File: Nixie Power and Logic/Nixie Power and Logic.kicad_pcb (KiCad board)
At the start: 2 copper layers, 172.7 x 111.8 mm, 54 parts, among them J1 Barrel_Jack, J10 Conn_01x20_Female, J11 Conn_01x20_Female, J12 Conn_01x20_Female, J13 LED Data, J2 Conn_01x02_Female, J3 Conn_01x02_Female, J4 Conn_01x02_Female, J5 Conn_01x02_Female, J6 Conn_01x02_Female, J7 Conn_01x02_Female, J8 Programming, J9 RTC, Q1 IRF740, Q2 MPSA92, Q3 BC547, SW1 SW_SPST, SW2 SW_SPST, SW3 Rotary_Encoder_EN11, SW4 Rotary_Encoder_EN11, SW5 Rotary_Encoder_EN11, SW6 SW_Reset, U1 ATmega168PA-PU, U10 74141, U11 L7805, U12 NE555, U2 74HC595, U3 74HC595, U4 74HC595, U5 74141, U6 74141, U7 74141, U8 74141, U9 74141, Y1 20MHz

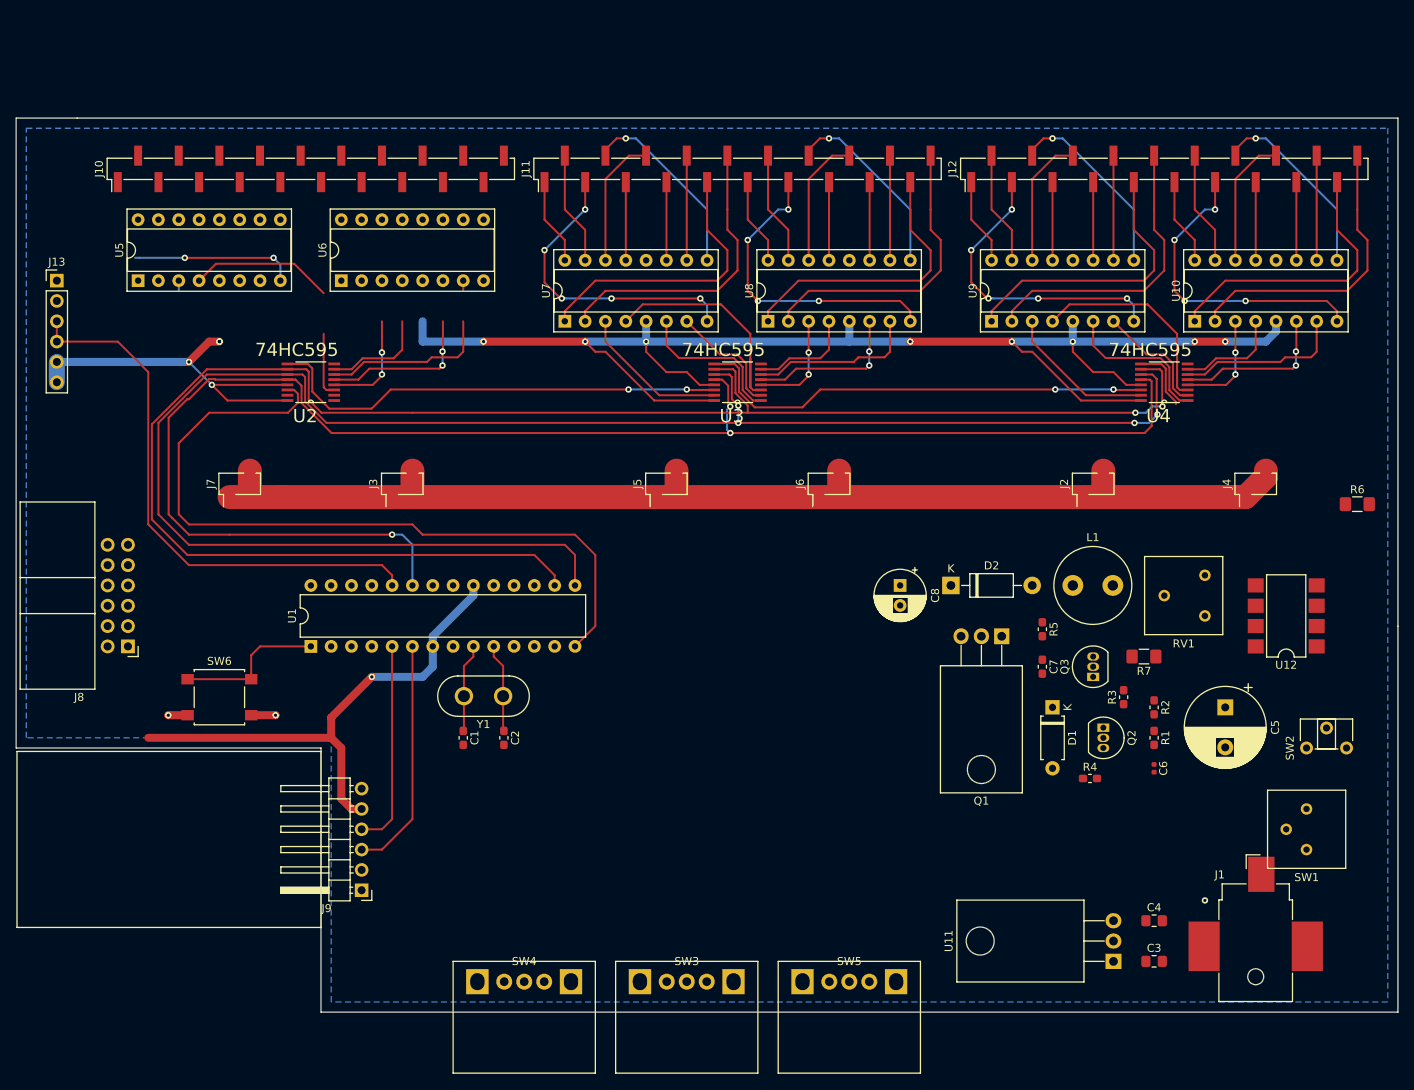
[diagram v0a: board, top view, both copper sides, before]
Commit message: Final V1.0 design. Different sized boards for top and bottom layer. Goal for v2.0 is to have matching top and bottom pcbas
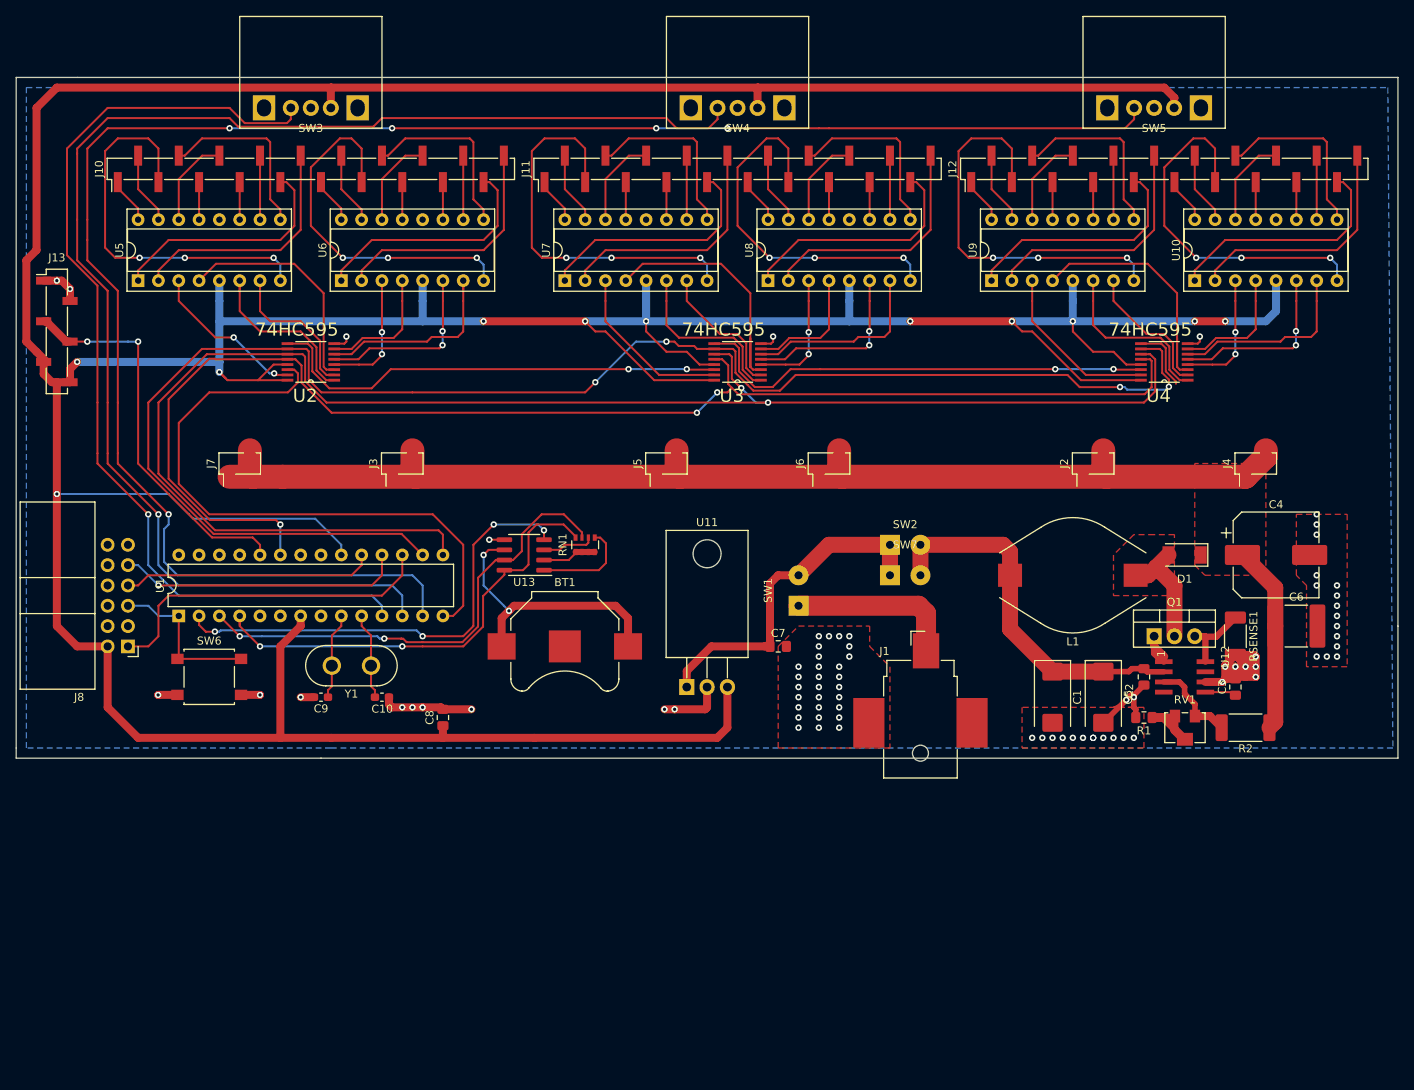
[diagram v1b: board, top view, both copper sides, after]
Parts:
- removed D2: uf4007, Diode_THT:D_DO-41_SOD81_P10.16mm_Horizontal
- removed J9: RTC, Connector_PinHeader_2.54mm:PinHeader_1x06_P2.54mm_Horizontal
- removed Q2: MPSA92, Package_TO_SOT_THT:TO-92_Inline
- removed Q3: BC547, Package_TO_SOT_THT:TO-92_Inline
- removed R3: 33k, Resistor_SMD:R_0603_1608Metric_Pad1.05x0.95mm_HandSolder
- removed R4, R5: 1k, Resistor_SMD:R_0603_1608Metric_Pad1.05x0.95mm_HandSolder
- removed R6: 220k, Resistor_SMD:R_1206_3216Metric_Pad1.42x1.75mm_HandSolder
- removed R7: 470, Resistor_SMD:R_1206_3216Metric_Pad1.42x1.75mm_HandSolder
- added BT1: Battery_Cell, Battery:BatteryHolder_Keystone_3000_1x12mm, F.Cu at (172.7, 85.1)
- added C1: 100Uf 35V, Capacitor_Tantalum_SMD:CP_EIA-7343-31_Kemet-D_Pad2.25x2.55mm_HandSolder, F.Cu at (233.7, 91.4)
- added C2: 100n, Capacitor_SMD:C_0805_2012Metric_Pad1.15x1.40mm_HandSolder, F.Cu at (245.1, 88.9)
- added RN1: R_Pack04, Resistor_SMD:R_Array_Convex_4x0603, F.Cu at (175.3, 72.4)
- added RSENSE1: 0R050, Resistor_SMD:R_2010_5025Metric_Pad1.52x2.65mm_HandSolder, F.Cu at (256.5, 83.8)
- added SW7: SW_Reset, Connector_Wire:SolderWirePad_1x02_P3.81mm_Drill1mm, F.Cu at (213.4, 76.2)
- added U13: DS3231MZ, Package_SO:SOIC-8_3.9x4.9mm_P1.27mm, F.Cu at (167.6, 73.7)
- C10: renamed from C2; value C -> 22pF
- C3: value 0.33uF -> 100n
- C4: value 0.1uF -> 4u7 250V; footprint Capacitor_SMD:C_0805_2012Metric_Pad1.15x1.40mm_HandSolder -> Capacitor_SMD:CP_Elec_10x14.3
- C5: value 470uF -> 10uF 25V; footprint Capacitor_THT:CP_Radial_D10.0mm_P5.00mm -> Capacitor_Tantalum_SMD:CP_EIA-7343-31_Kemet-D_Pad2.25x2.55mm_HandSolder
- C6: value 2n2 -> 100n 250V; footprint Capacitor_SMD:C_0402_1005Metric -> Capacitor_SMD:C_2220_5650Metric_Pad1.97x5.40mm_HandSolder
- C7: value 47pF -> 0.33uF; footprint Capacitor_SMD:C_0603_1608Metric_Pad1.05x0.95mm_HandSolder -> Capacitor_SMD:C_0805_2012Metric_Pad1.15x1.40mm_HandSolder
- C8: value 1uF 350V -> 0.1uF; footprint Capacitor_THT:CP_Radial_D6.3mm_P2.50mm -> Capacitor_SMD:C_0805_2012Metric_Pad1.15x1.40mm_HandSolder
- C9: renamed from C1; value C -> 22pF
- D1: value 1n914 -> ES2F; footprint Diode_THT:D_A-405_P7.62mm_Horizontal -> Nixie Power and Logic:D_SOD-214AA
- J13: footprint Connector_PinHeader_2.54mm:PinHeader_1x06_P2.54mm_Vertical -> Connector_PinSocket_2.54mm:PinSocket_1x06_P2.54mm_Vertical_SMD_Pin1Left
- L1: footprint Inductor_THT:L_Radial_D9.5mm_P5.00mm_Fastron_07HVP -> Inductor_SMD:L_Bourns_SDR1806
- Q1: value IRF740 -> IRF644; footprint Package_TO_SOT_THT:TO-220-3_Horizontal_TabDown -> Package_TO_SOT_THT:TO-220-3_Vertical
- R1: footprint Resistor_SMD:R_0603_1608Metric_Pad1.05x0.95mm_HandSolder -> Resistor_SMD:R_0805_2012Metric_Pad1.15x1.40mm_HandSolder
- R2: value 1k -> 1M5; footprint Resistor_SMD:R_0603_1608Metric_Pad1.05x0.95mm_HandSolder -> Resistor_SMD:R_2512_6332Metric_Pad1.52x3.35mm_HandSolder
- RV1: value 1k -> 5k; footprint Potentiometer_THT:Potentiometer_Bourns_3386F_Vertical -> Potentiometer_SMD:Potentiometer_Bourns_3214W_Vertical
- SW1: value SW_SPST -> Main Power Switch; footprint Potentiometer_THT:Potentiometer_Bourns_3386P_Vertical -> Connector_Wire:SolderWirePad_1x02_P3.81mm_Drill1mm
- SW2: value SW_SPST -> 180V Switch; footprint Potentiometer_THT:Potentiometer_Piher_PT-6-H_Horizontal -> Connector_Wire:SolderWirePad_1x02_P3.81mm_Drill1mm
- U12: value NE555 -> MAX171; footprint Package_DIP:SMDIP-8_W7.62mm -> Nixie Power and Logic:SOIC−8-NARROW
- Y1: value 20MHz -> 16MHz
- moved SW3 118.9 mm to (141.0, 17.8), turned to 180 degrees
- moved SW5 115.7 mm to (246.4, 17.8), turned to 180 degrees
- moved SW4 112.4 mm to (194.3, 17.8), turned to 180 degrees
- moved SW1 68.4 mm to (201.9, 80.0), turned to 90 degrees
- moved U11 63.4 mm to (188.0, 90.2), turned to 0 degrees
- moved C8 59.5 mm to (157.5, 94.0), turned to 90 degrees
- moved SW2 57.9 mm to (213.4, 72.4), turned to 0 degrees
- moved J1 50.4 mm to (217.2, 91.4)
- moved C4 48.2 mm to (261.6, 73.7)
- moved C3 35.8 mm to (256.5, 90.2), turned to 90 degrees
- moved C7 33.1 mm to (199.4, 85.1), turned to 0 degrees
- moved D1 25.2 mm to (250.2, 73.7), turned to 180 degrees
- moved C6 25.1 mm to (264.2, 82.5), turned to 0 degrees
- moved RV1 19.2 mm to (250.2, 95.2), turned to 0 degrees
- moved Q1 19.0 mm to (246.4, 83.8), turned to 0 degrees
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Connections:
- C10 pad 2: GND -> Net-(C10-Pad2)
- C4 pad 1: +5V -> /180V
- C5 pad 1: Net-(C5-Pad1) -> /vcc
- C6 pad 1: Net-(C6-Pad1) -> /180V
- C8 pad 1: /180V -> +5V
- C9 pad 2: GND -> Net-(C10-Pad2)
- D1 pad 1: Net-(D1-Pad1) -> /180V
- L1 pad 1: Net-(D2-Pad2) -> Net-(D1-Pad2)
- L1 pad 2: Net-(C5-Pad1) -> /vcc
- Q1 pad 1: Net-(D1-Pad1) -> Net-(Q1-Pad1)
- Q1 pad 2: Net-(D2-Pad2) -> Net-(D1-Pad2)
- Q1 pad 3: GND -> Net-(Q1-Pad3)
- R1 pad 2: Net-(C6-Pad1) -> GND
- R2 pad 1: Net-(C5-Pad1) -> /180V
- R2 pad 2: Net-(R1-Pad1) -> Net-(R2-Pad2)
- RV1 pad 1: Net-(R6-Pad2) -> Net-(R2-Pad2)
- RV1 pad 2: Net-(Q3-Pad2) -> Net-(R1-Pad1)
- RV1 pad 3: Net-(R7-Pad1) -> Net-(R1-Pad1)
- SW1 pad 2: Net-(C3-Pad1) -> Net-(C7-Pad1)
- SW2 pad 1: Net-(C3-Pad1) -> Net-(C7-Pad1)
- SW2 pad 2: Net-(C5-Pad1) -> /vcc
- SW6 pad 2: GND -> Net-(C10-Pad2)
- U1 pad 2: Net-(U1-Pad2) -> ~RTCRST
- U1 pad 3: Net-(U1-Pad3) -> RTCSDA
- U1 pad 4: Net-(U1-Pad4) -> RTCSCL
- U11 pad 1: Net-(C3-Pad1) -> Net-(C7-Pad1)
- U12 pad 1: GND -> Net-(Q1-Pad1)
- U12 pad 2: Net-(C6-Pad1) -> /vcc
- U12 pad 3: Net-(D1-Pad2) -> Net-(R2-Pad2)
- U12 pad 4: Net-(C5-Pad1) -> SHDN
- U12 pad 5: Net-(Q3-Pad1) -> Net-(C3-Pad1)
- U12 pad 6: Net-(C6-Pad1) -> GND
- U12 pad 7: Net-(R1-Pad1) -> Net-(U12-Pad7)
- U12 pad 8: Net-(C5-Pad1) -> Net-(Q1-Pad3)
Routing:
- net +5V: track 291.9 -> 640.9 mm, vias 13 -> 11
- net Net-(SW5-Pad3): track 0.00 -> 227.2 mm, vias 0 -> 5
- net Net-(SW4-Pad3): track 0.00 -> 175.8 mm, vias 0 -> 1
- net Net-(SW3-Pad3): track 0.00 -> 121.3 mm, vias 0 -> 1
- net GND: track 5.47 -> 77.0 mm, vias 3 -> 77
- net RTCSDA: track 0.00 -> 59.7 mm, vias 0 -> 2
- net ~RTCRST: track 0.00 -> 58.2 mm, vias 0 -> 4
- net RTCSCL: track 0.00 -> 57.4 mm, vias 0 -> 2
- net /vcc: track 0.00 -> 46.8 mm
- net Net-(C7-Pad1): track 0.00 -> 46.2 mm
- net Net-(J10-Pad13): track 0.00 -> 45.5 mm, vias 0 -> 3
- net /MOSI: track 0.00 -> 42.7 mm
- net /MISO: track 0.00 -> 35.9 mm, vias 0 -> 1
- net Net-(BT1-Pad1): track 0.00 -> 35.3 mm, vias 0 -> 2
- net /SCK: track 0.00 -> 31.5 mm
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- added copper zone on F.Cu, net /180V
- added copper zone on F.Cu, net GND
- added copper zone on F.Cu, net Net-(D1-Pad2)
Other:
- board size 172.7 x 111.8 mm -> 172.7 x 85.1 mm
